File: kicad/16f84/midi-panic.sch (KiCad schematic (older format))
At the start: 20 parts

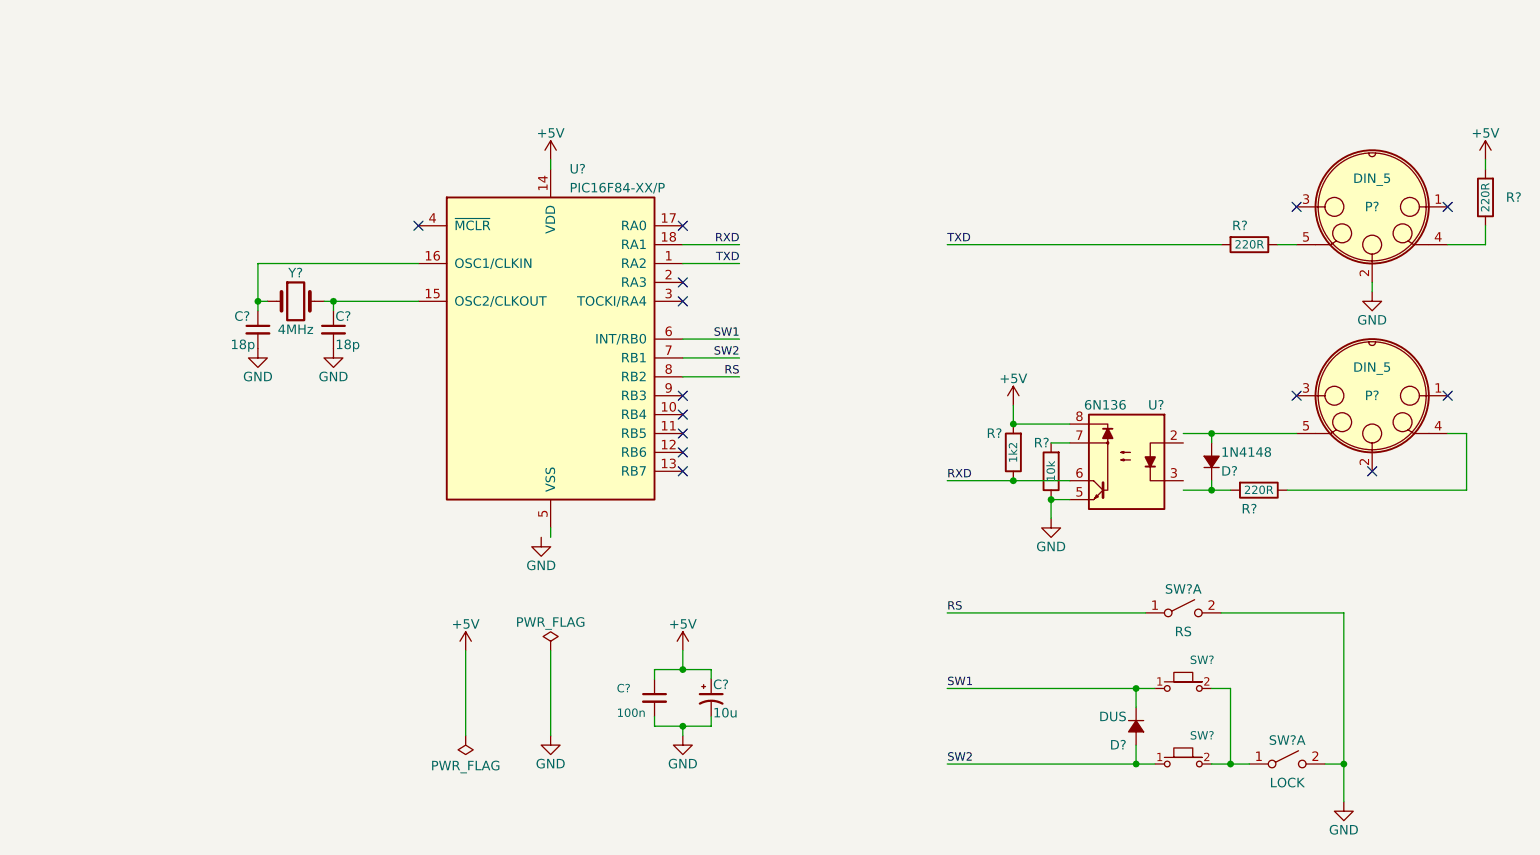
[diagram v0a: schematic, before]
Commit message: Update schematics to KiCad 5. Update wks files.
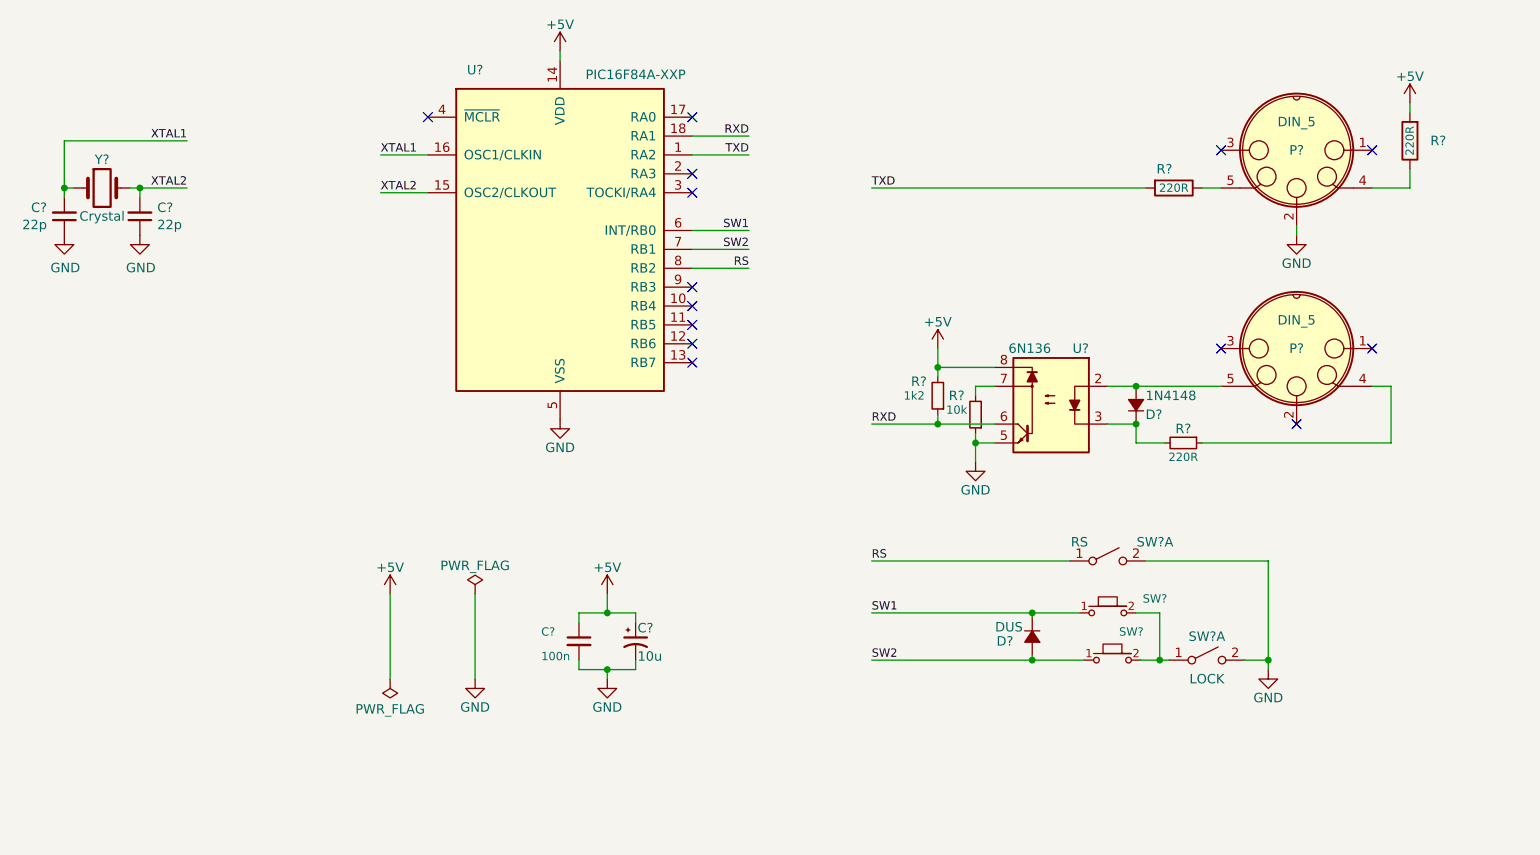
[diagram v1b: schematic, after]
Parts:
- removed C?: 100n, Capacitors_SMD:C_1206_HandSoldering, symbol C_Small
- removed C?: 10u, symbol CP1_Small
- removed C? (x2): 18p, symbol C_Small
- removed D?: 1N4148, symbol D_Small_ALT
- removed D?: DUS, symbol D_Small_ALT
- removed P? (x2): DIN_5, symbol DIN_5
- removed R? (x3): 220R, Resistors_SMD:R_1206_HandSoldering, symbol R
- removed R?: 1k2, Resistors_SMD:R_1206_HandSoldering, symbol R
- removed R?: 10k, Resistors_SMD:R_1206_HandSoldering, symbol R
- removed SW? (x2): PUSH_BUTTON, Buttons_Switches_ThroughHole:SW_PUSH-12mm, symbol PUSH_BUTTON-RESCUE-tinyVT
- removed SW?: RS, symbol SW_DPST_x2
- removed SW?: LOCK, symbol SW_DPST_x2
- removed U?: PIC16F84-XX/P, symbol PIC16F84-XX/P
- removed U?: 6N136, Housings_DIP:DIP-8_W7.62mm, symbol 6N136
- removed Y?: 4MHz, symbol Crystal
- added C?: 100n, Capacitors_SMD:C_1206_HandSoldering, symbol midi-panic-rescue:C_Small
- added C?: 10u, symbol midi-panic-rescue:CP1_Small
- added C? (x2): 22p, symbol Device:C_Small
- added D?: 1N4148, symbol midi-panic-rescue:D_Small_ALT
- added D?: DUS, symbol midi-panic-rescue:D_Small_ALT
- added P? (x2): DIN_5, symbol midi-panic-rescue:DIN_5
- added R? (x2): 220R, Resistors_SMD:R_1206_HandSoldering, symbol midi-panic-rescue:R
- added R?: 220R, symbol Device:R_Small
- added R?: 10k, symbol Device:R_Small
- added R?: 1k2, symbol Device:R_Small
- added SW? (x2): PUSH_BUTTON, Buttons_Switches_ThroughHole:SW_PUSH-12mm, symbol midi-panic-rescue:PUSH_BUTTON-RESCUE-tinyVT
- added SW?: RS, symbol midi-panic-rescue:SW_DPST_x2
- added SW?: LOCK, symbol midi-panic-rescue:SW_DPST_x2
- added U?: 6N136, Housings_DIP:DIP-8_W7.62mm, symbol midi-panic-rescue:6N136
- added U?: PIC16F84A-XXP, symbol MCU_Microchip_PIC16:PIC16F84A-XXP
- added Y?: Crystal, symbol Device:Crystal
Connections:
- net labels added: XTAL1, XTAL2
- wire segments 52 -> 67
